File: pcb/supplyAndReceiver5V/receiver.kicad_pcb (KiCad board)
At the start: 2 copper layers, 20 x 16 mm, 7 parts, among them J1 WAGO 2061-602, J2 har-flexicon 2,54 MSH-4, J3 Conn_01x05_Socket, J4 Conn_01x02, U1 SP485CN

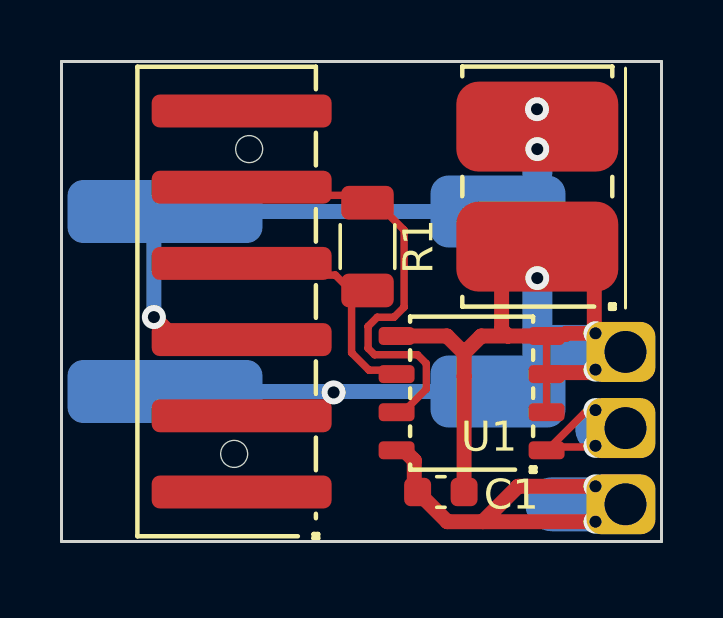
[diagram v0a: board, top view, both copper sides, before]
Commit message: Add receiver for IKEA Metod cupboard
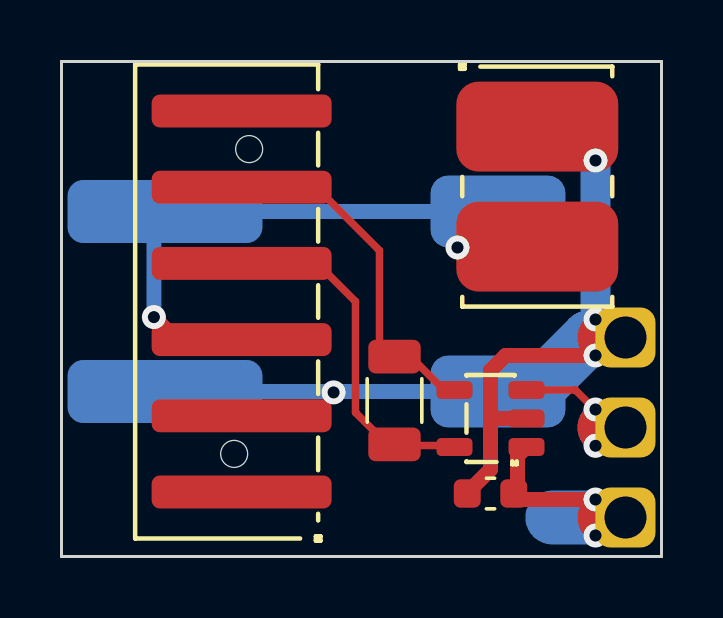
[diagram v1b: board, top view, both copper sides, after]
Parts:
- removed U1: SP485CN, local:SP485
- added U2: ISL3280ExHZ, local:ISL3280E, F.Cu at (144.3, 103.9)
- J3: footprint local:HolesL -> local:SolderHoles3pin10mm
- J4: value Conn_01x02 -> Kyocera-009176002001906
- moved R1 5.21 mm to (141.1, 103.3)
- moved C1 1.66 mm to (144.3, 106.4), turned to 180 degrees
- turned J4 to -90 degrees
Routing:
- net +5V: track 19.0 -> 8.96 mm
- net GND: track 40.2 -> 33.1 mm
- net RS485_A: track 8.21 -> 12.1 mm
- net RS485_B: track 19.4 -> 16.2 mm
- net +15V: track 20.2 -> 18.0 mm, vias 3 -> 2
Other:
- board size 20 x 16 mm -> 20 x 16.5 mm

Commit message: Use ISL3280E
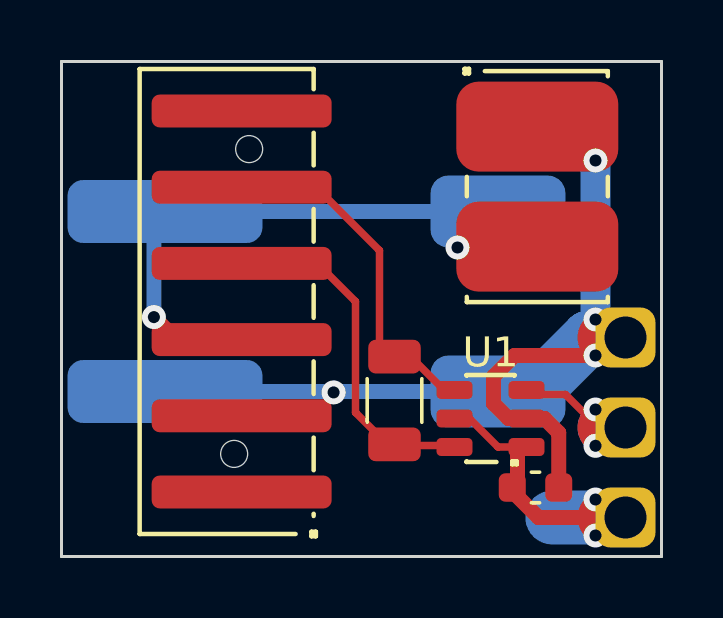
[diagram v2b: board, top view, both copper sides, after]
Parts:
- U1: renamed from U2; value ISL3280ExHZ -> ISL3281E; footprint local:ISL3280E -> local:ISL3281E
- moved C1 1.51 mm to (145.8, 106.2), turned to 0 degrees
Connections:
- U1 pad 5: RS485_A -> +5V
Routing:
- net +5V: track 8.96 -> 13.4 mm
- net DATA: track 8.35 -> 9.59 mm

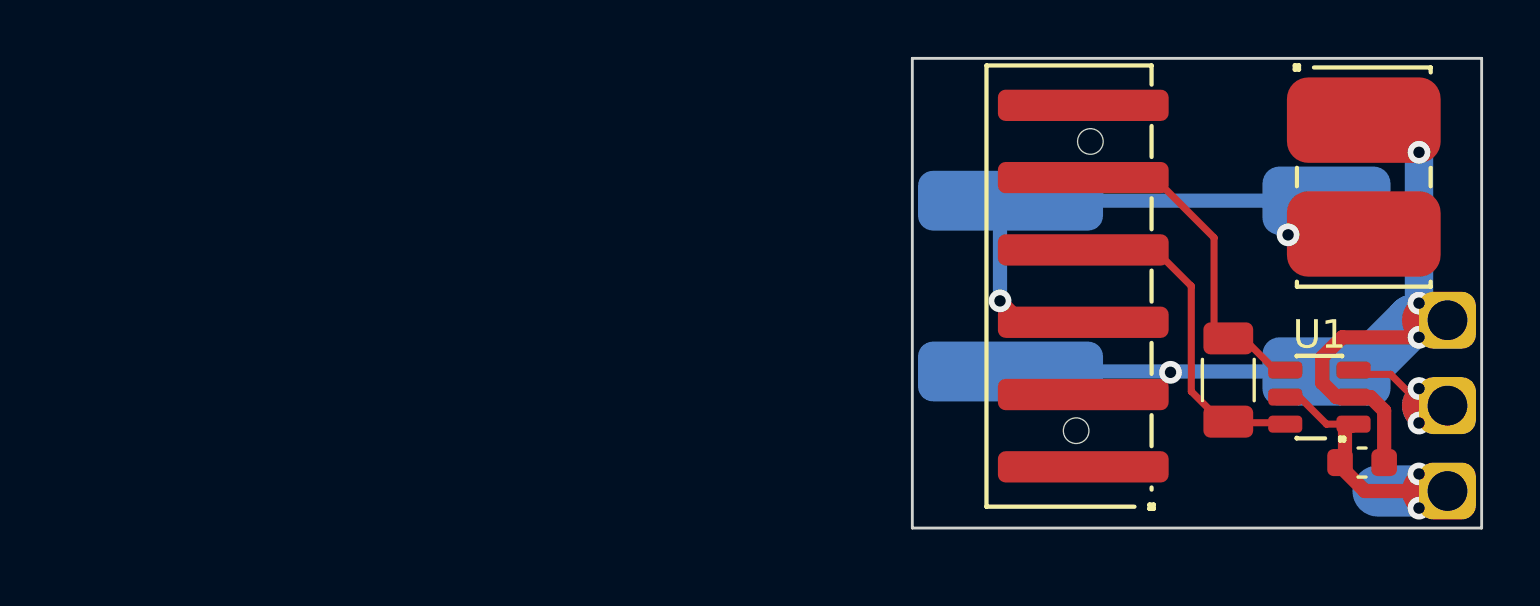
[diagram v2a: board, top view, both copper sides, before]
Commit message: New pin ordering for Harting connector
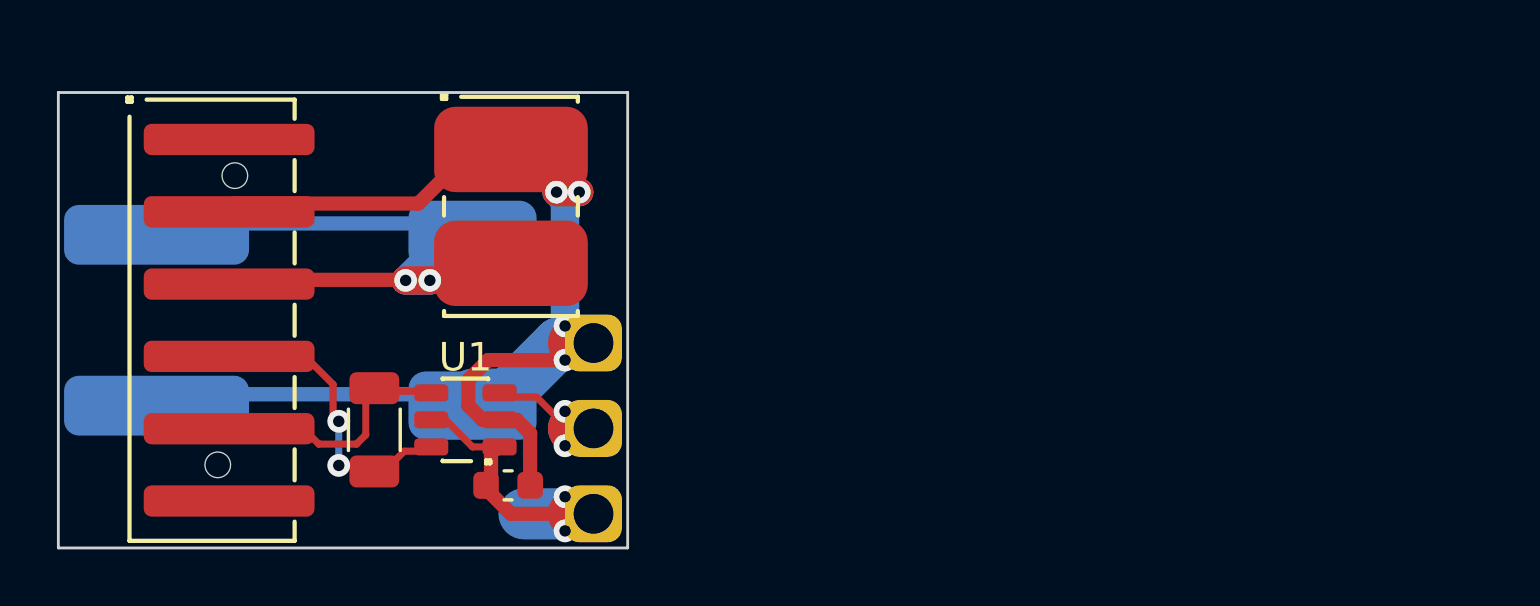
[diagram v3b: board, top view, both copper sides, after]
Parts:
- moved R1 30.1 mm to (111.1, 105.0)
- moved J2 30.0 mm to (106.0, 101.2), turned to -90 degrees
- moved J1 30.0 mm to (108.2, 101.2)
- moved C1 30.0 mm to (115.8, 107.0)
- moved J3 30.0 mm to (118.8, 105.0)
- moved U1 30.0 mm to (114.3, 104.7)
- moved J4 30.0 mm to (115.9, 97.2)
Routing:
- net GND: track 32.7 -> 44.2 mm
- net +15V: track 18.0 -> 25.7 mm
- net RS485_B: track 16.2 -> 9.05 mm
- net RS485_A: track 12.1 -> 10.7 mm, vias 0 -> 2
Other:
- board size 20 x 16.5 mm -> 20 x 16 mm
- board text added: "LED Strip"
